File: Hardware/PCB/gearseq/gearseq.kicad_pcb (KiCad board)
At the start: 2 copper layers, 209.5 x 165 mm, 85 parts, among them J1 AudioJack2_SwitchT, J10 Conn_01x11, J11 Conn_01x04, J12 AudioJack2, J13 AudioJack2, J14 Conn_01x11, J15 2_pin_Molex_connector, J16 2_pin_Molex_connector, J17 2_pin_Molex_header, J18 2_pin_Molex_connector, J2 AudioJack2_SwitchT, J3 AudioJack2, J4 AudioJack2, J5 Synth_power_2x5, J6 2_pin_Molex_header, J7 2_pin_Molex_header, J8 AudioJack2_SwitchT, J9 AudioJack2_SwitchT, Q1 2N3904, Q2 2N3904, SW1 SW_Push_black, SW2 SW_Push_red, SW3 SW_SPST, U2 L78L05_TO92

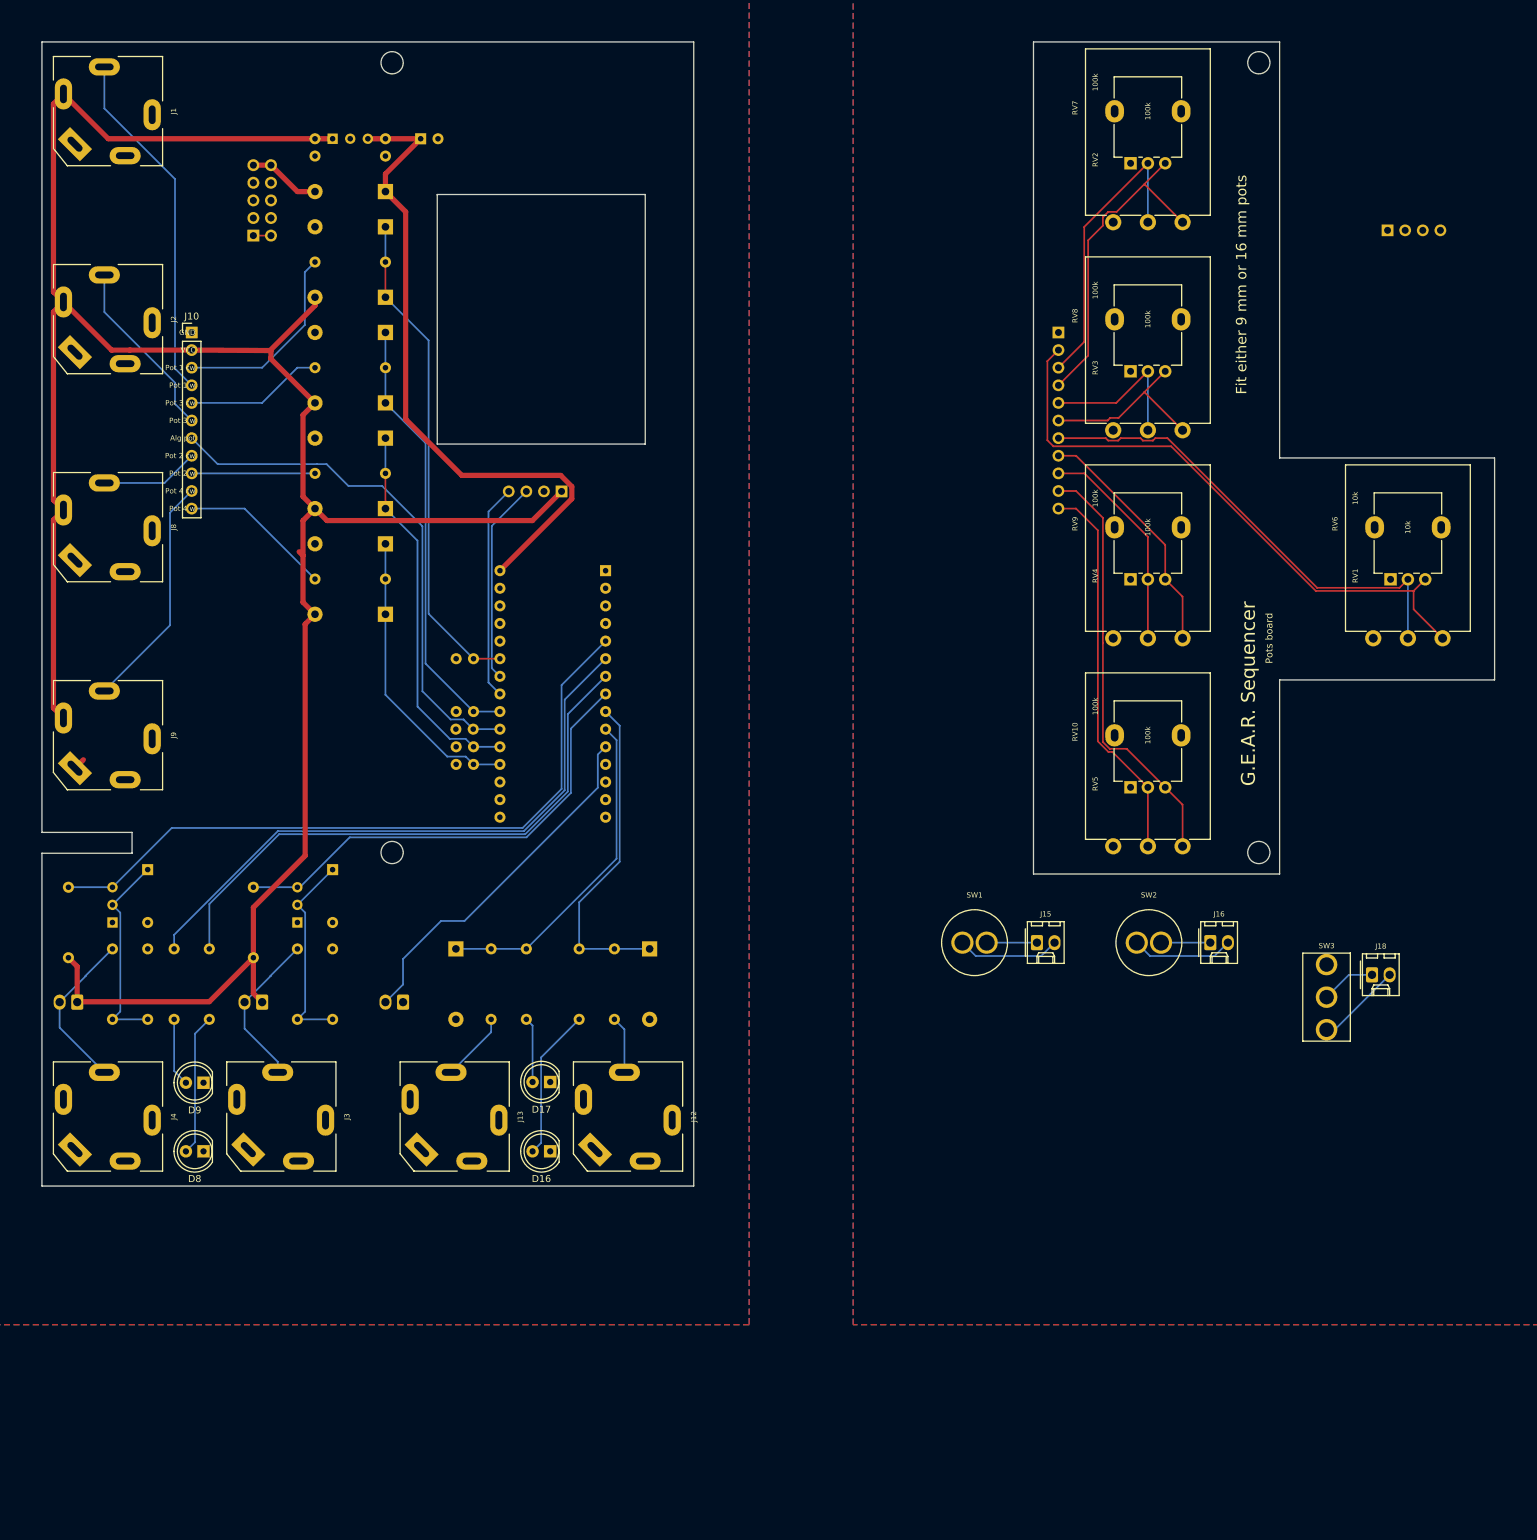
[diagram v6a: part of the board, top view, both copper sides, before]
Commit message: Final pre fab tweaks, correct oversize LED footprint
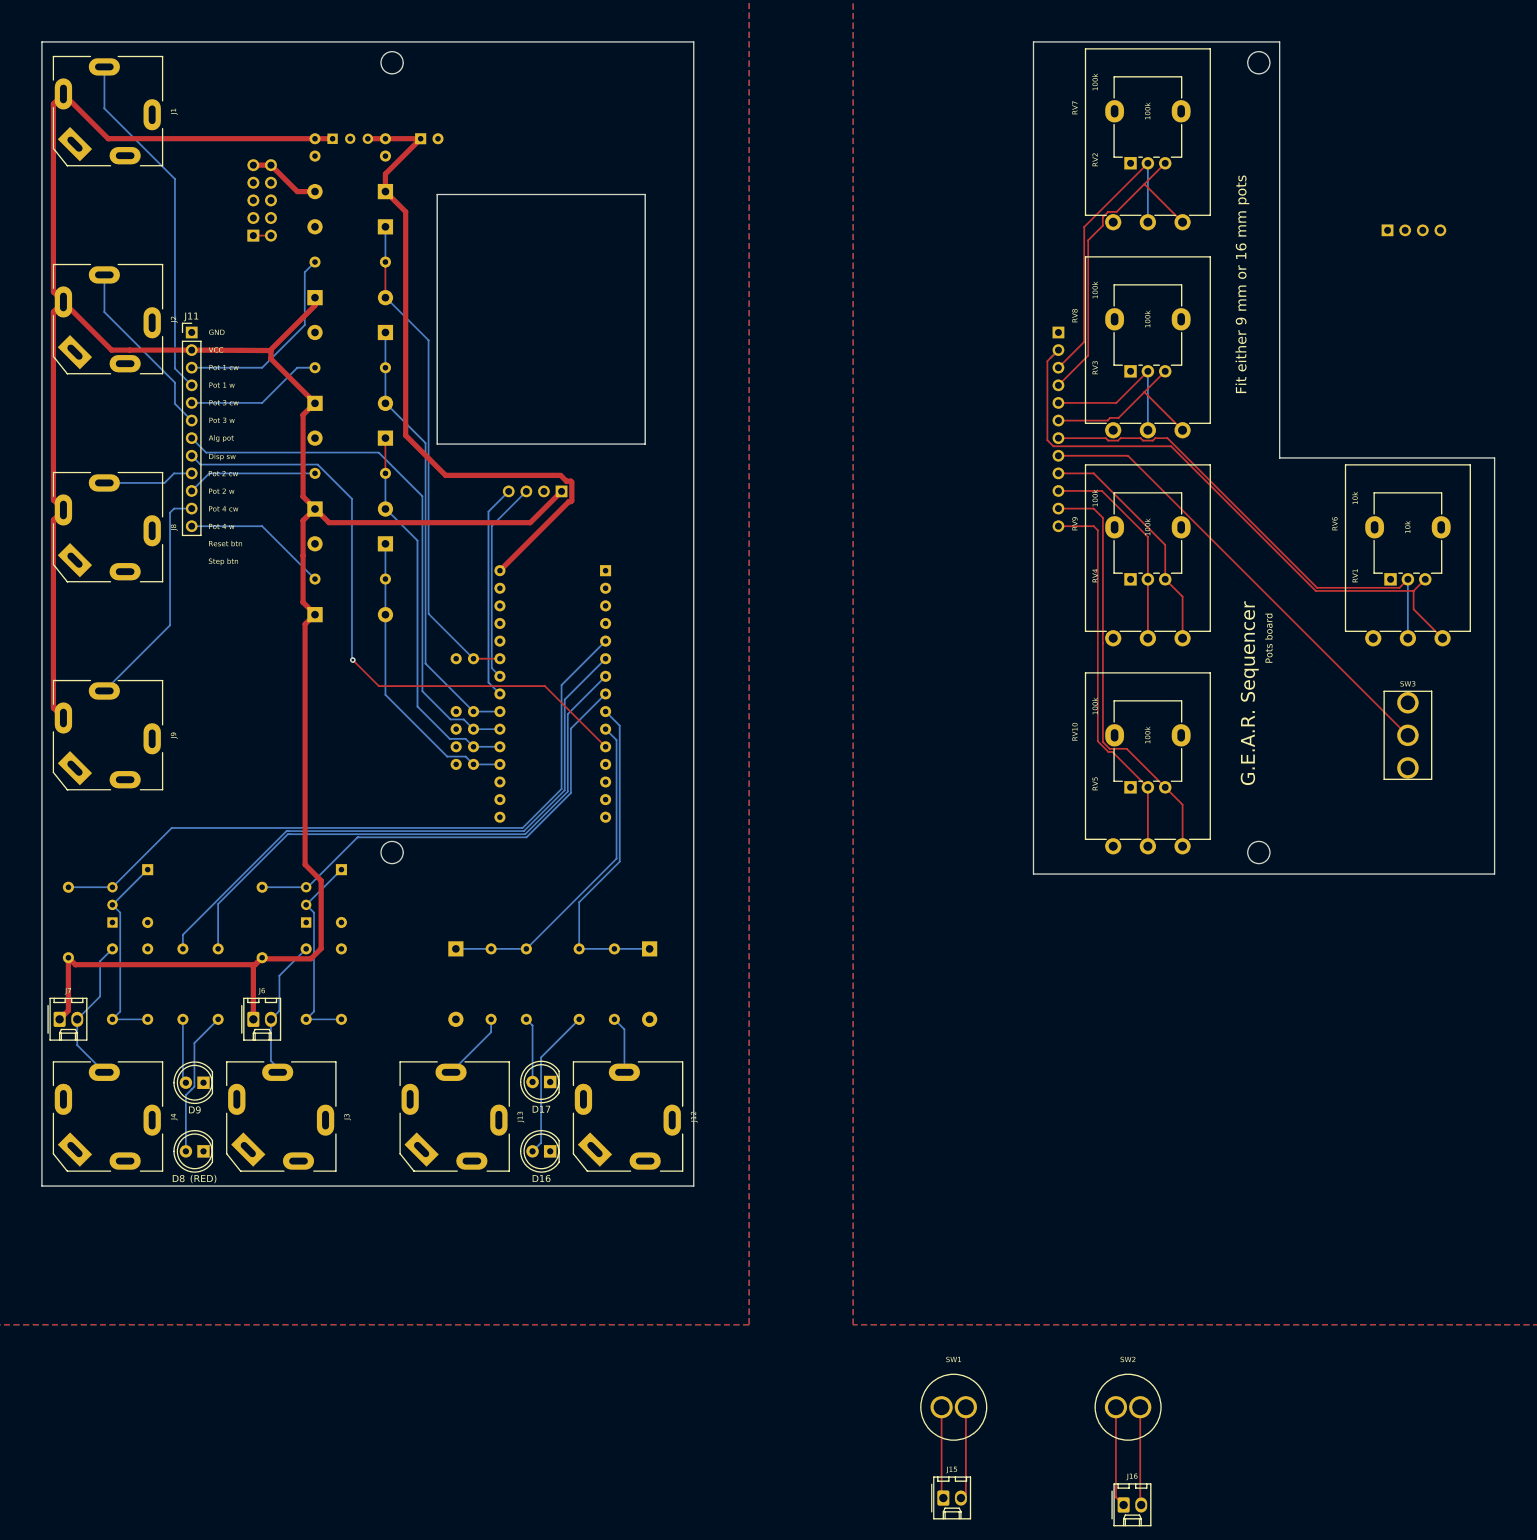
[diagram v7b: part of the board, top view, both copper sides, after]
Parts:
- removed J17: 2_pin_Molex_header, ao_tht:Molex_KK-254_AE-6410-02A_1x02_P2.54mm_Vertical
- removed J18: 2_pin_Molex_connector, ao_tht:Molex_KK-254_AE-6410-02A_1x02_P2.54mm_Vertical
- C2: renamed from C4; value 100nF -> 10nF
- C3: renamed from C5; value 100nF -> 10nF
- C6, C7, C8: value 100nF -> 10nF
- J11: renamed from J10; value Conn_01x11 -> Conn_01x12; footprint Connector_PinHeader_2.54mm:PinHeader_1x11_P2.54mm_Vertical -> Connector_PinHeader_2.54mm:PinHeader_1x12_P2.54mm_Vertical
- J14: value Conn_01x11 -> Conn_01x12; footprint Connector_PinSocket_2.54mm:PinSocket_1x11_P2.54mm_Vertical -> Connector_PinSocket_2.54mm:PinSocket_1x12_P2.54mm_Vertical
- J6, J7: moved to F.Cu
- moved J16 82.1 mm to (182.0, 233.0)
- moved J15 81.2 mm to (156.0, 232.0)
- moved SW1 67.1 mm to (157.5, 218.9)
- moved SW2 67.1 mm to (182.6, 218.9)
- moved SW3 39.5 mm to (223.0, 122.0)
- moved D10 10.2 mm to (65.4, 89.4), turned to 0 degrees
- moved D12 10.2 mm to (65.4, 104.6), turned to 0 degrees
- moved D4 10.2 mm to (65.4, 58.9), turned to 0 degrees
- moved D6 10.2 mm to (65.4, 74.1), turned to 0 degrees
- moved J7 3.55 mm to (28.6, 163.0), turned to 0 degrees
- moved J6 2.79 mm to (56.5, 163.0), turned to 0 degrees
- moved C8 2.54 mm to (88.2, 121.1), turned to 180 degrees
- moved D2 1.27 mm to (69.2, 141.4)
- moved Q1 1.27 mm to (64.1, 149.0)
- moved R1 1.27 mm to (64.1, 163.0)
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- renumbered C2 to C4, C3 to C5, D3 to D1, D1 to D2, D2 to D3, GRAF3 to GRAF2, GRAF4 to GRAF3, GRAF2 to GRAF4, H3 to H2, H4 to H3, H6 to H4, J11 to J10, R8 to R10, R9 to R7, R10 to R8, R7 to R9, U2 to U1
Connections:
- A1 pad 11: Net-(A1-Pad11) -> DISP_SW
- C8 pad 1: GND -> POT_ALG
- C8 pad 2: POT_ALG -> GND
- D10 pad 1: CV_3 -> +5V
- D10 pad 2: +5V -> CV_3
- D12 pad 1: CV_4 -> +5V
- D12 pad 2: +5V -> CV_4
- D4 pad 1: CV_1 -> +5V
- D4 pad 2: +5V -> CV_1
- D6 pad 1: CV_2 -> +5V
- D6 pad 2: +5V -> CV_2
- J11 pad 10: POT_4_CW -> POT_3_W
- J11 pad 11: POT_4_W -> POT_4_CW
- J11 pad 8: POT_3_CW -> DISP_SW
- J11 pad 9: POT_3_W -> POT_3_CW
- J14 pad 10: POT_4_CW_P -> POT_3_W_P
- J14 pad 11: POT_4_W_P -> POT_4_CW_P
- J14 pad 8: POT_3_CW_P -> DISP_SW_P
- J14 pad 9: POT_3_W_P -> POT_3_CW_P
- SW1 pad 1: Net-(J15-Pad2) -> Net-(J15-Pad1)
- SW1 pad 2: Net-(J15-Pad1) -> Net-(J15-Pad2)
- SW2 pad 1: Net-(J16-Pad2) -> Net-(J16-Pad1)
- SW2 pad 2: Net-(J16-Pad1) -> Net-(J16-Pad2)
- SW3 pad 1: Net-(J18-Pad2) -> GND1
- SW3 pad 2: Net-(J18-Pad1) -> DISP_SW_P
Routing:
- net DISP_SW: track 0.00 -> 90.6 mm, vias 0 -> 1
- net DISP_SW_P: track 0.00 -> 67.1 mm
- net Net-(A1-Pad11): track 52.0 -> 0.00 mm
- net Net-(J18-Pad2): track 12.4 -> 0.00 mm
- net +5V: track 356.4 -> 367.3 mm
- net Net-(J18-Pad1): track 7.89 -> 0.00 mm
- net Net-(J16-Pad1): track 7.10 -> 14.6 mm
- net Net-(J15-Pad1): track 7.25 -> 13.2 mm
- net /RESET_J: track 22.9 -> 20.3 mm
- net POT_ALG: track 75.8 -> 78.3 mm
- net /CLK_IN_J: track 23.6 -> 21.5 mm
- net +12V: track 95.8 -> 97.7 mm
- net GND: track 5.58 -> 3.86 mm
- net +5V_1: track 86.4 -> 88.1 mm
- net Net-(J15-Pad2): track 14.9 -> 13.4 mm
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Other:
- outline, holes or cut-outs redrawn
- board text added: "(RED)"
- board text added: "Disp sw"
- board text added: "Reset btn"
- board text added: "Step btn"
- board text removed: "Reset button"
- board text removed: "Step button"

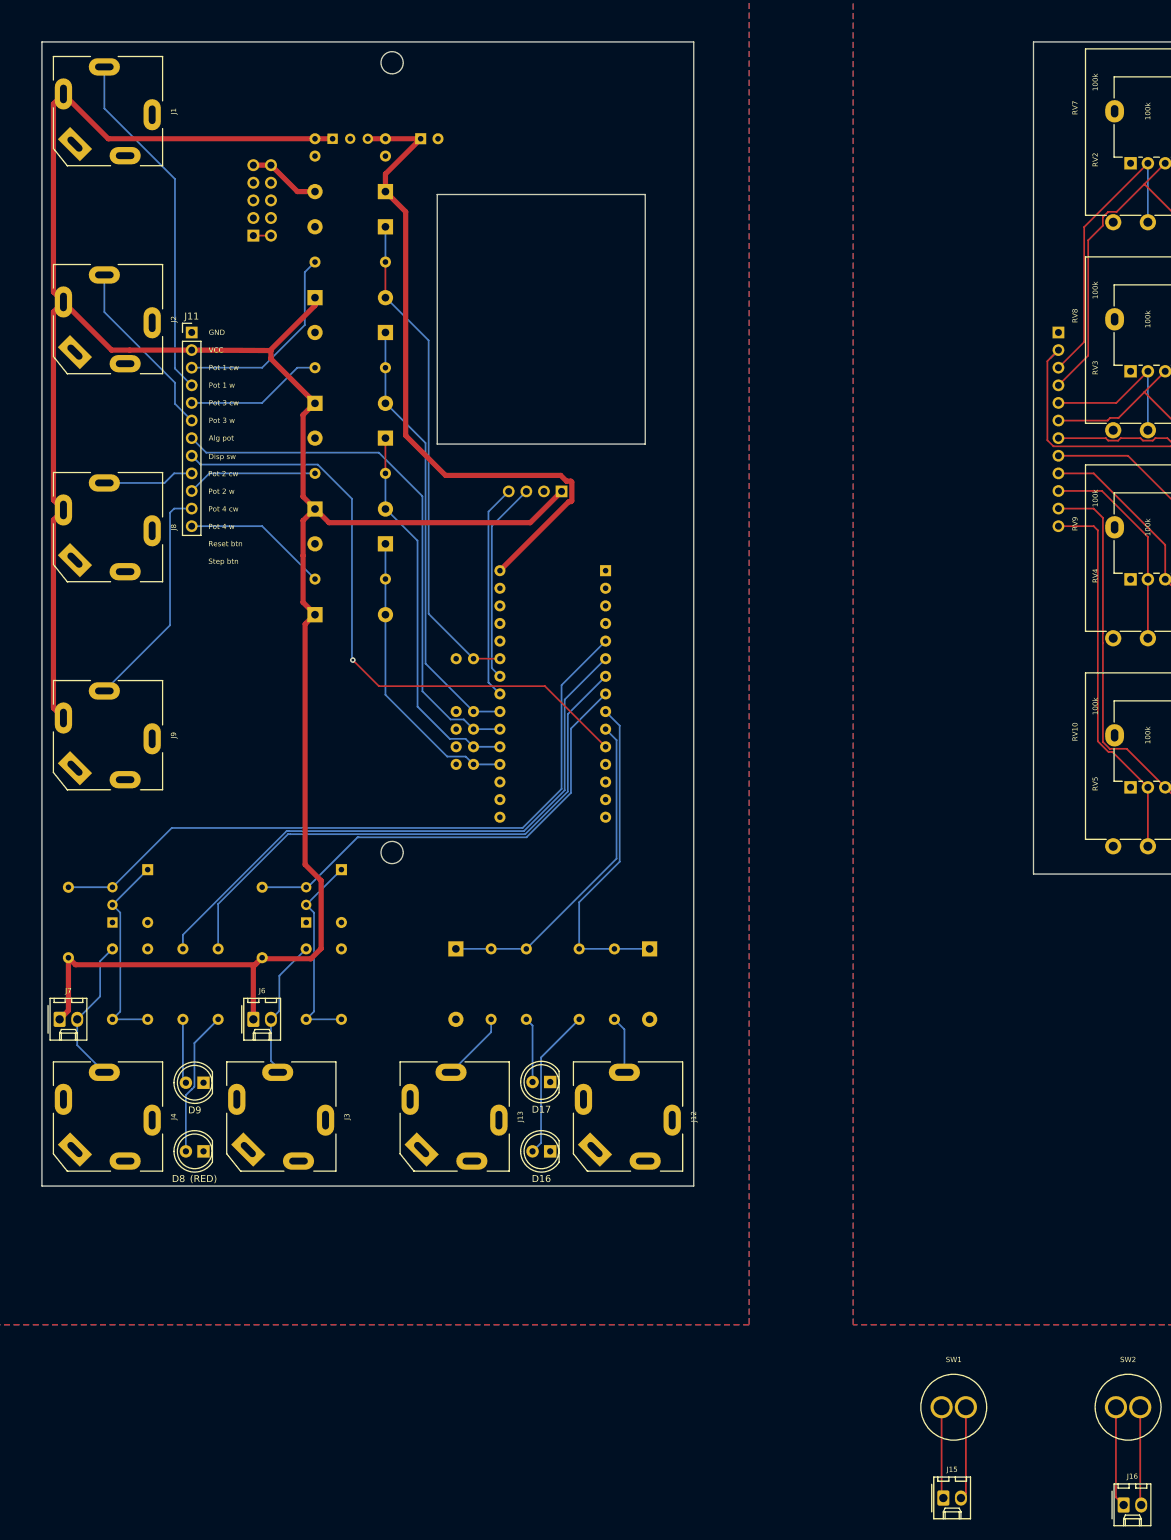
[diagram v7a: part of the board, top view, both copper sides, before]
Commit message: Update docs, generate Gerbers, change PCB hole to notch
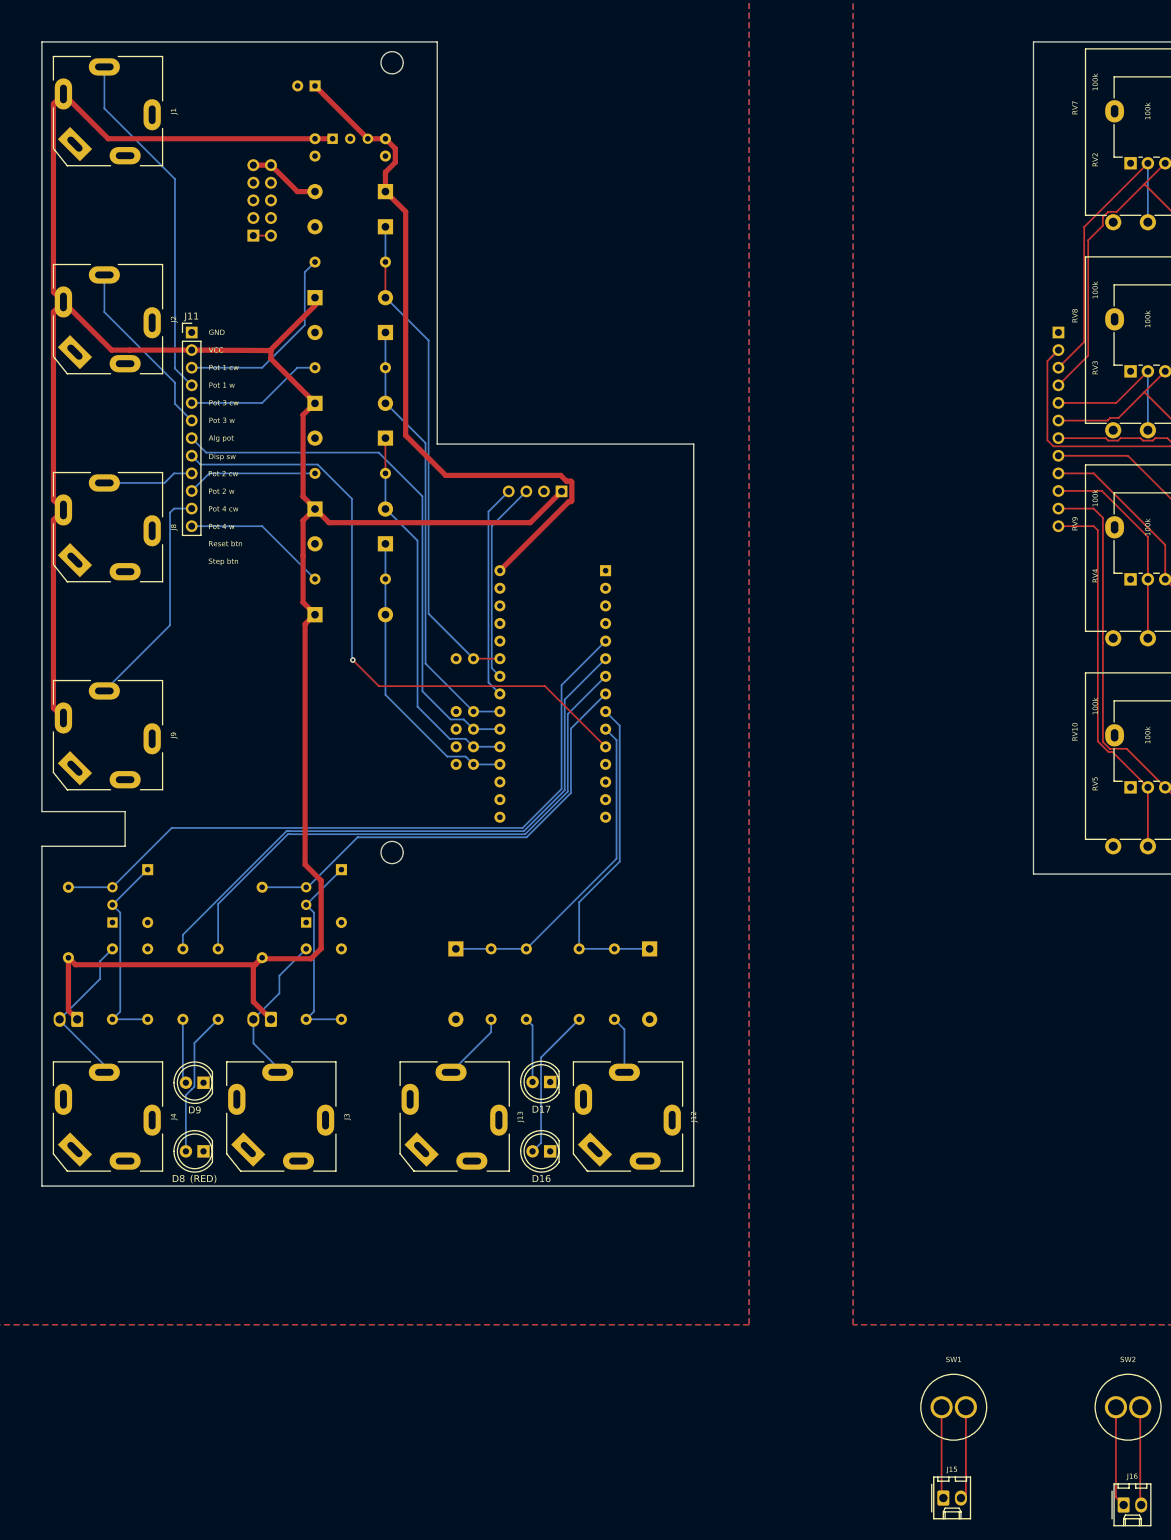
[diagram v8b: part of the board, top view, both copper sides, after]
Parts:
- J6, J7: moved to B.Cu
- moved C1 17.0 mm to (65.4, 28.3), turned to 180 degrees
- moved J6 2.54 mm to (59.0, 163.0), turned to 180 degrees
- moved J7 2.54 mm to (31.1, 163.0), turned to 180 degrees
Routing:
- net +12V: track 97.7 -> 102.5 mm
- net /CLK_IN_J: track 21.5 -> 23.6 mm
- net /RESET_J: track 20.3 -> 22.4 mm
- net +5V: track 367.3 -> 368.4 mm
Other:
- outline, holes or cut-outs redrawn
